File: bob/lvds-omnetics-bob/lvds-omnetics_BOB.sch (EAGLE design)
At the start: 33 parts, among them U1 SN65LVDS1, U2 SN65LVDS2, U3 SN65LVDS1, U4 SN65LVDS2, U5 SN65LVDS1, U6 SN65LVDS1

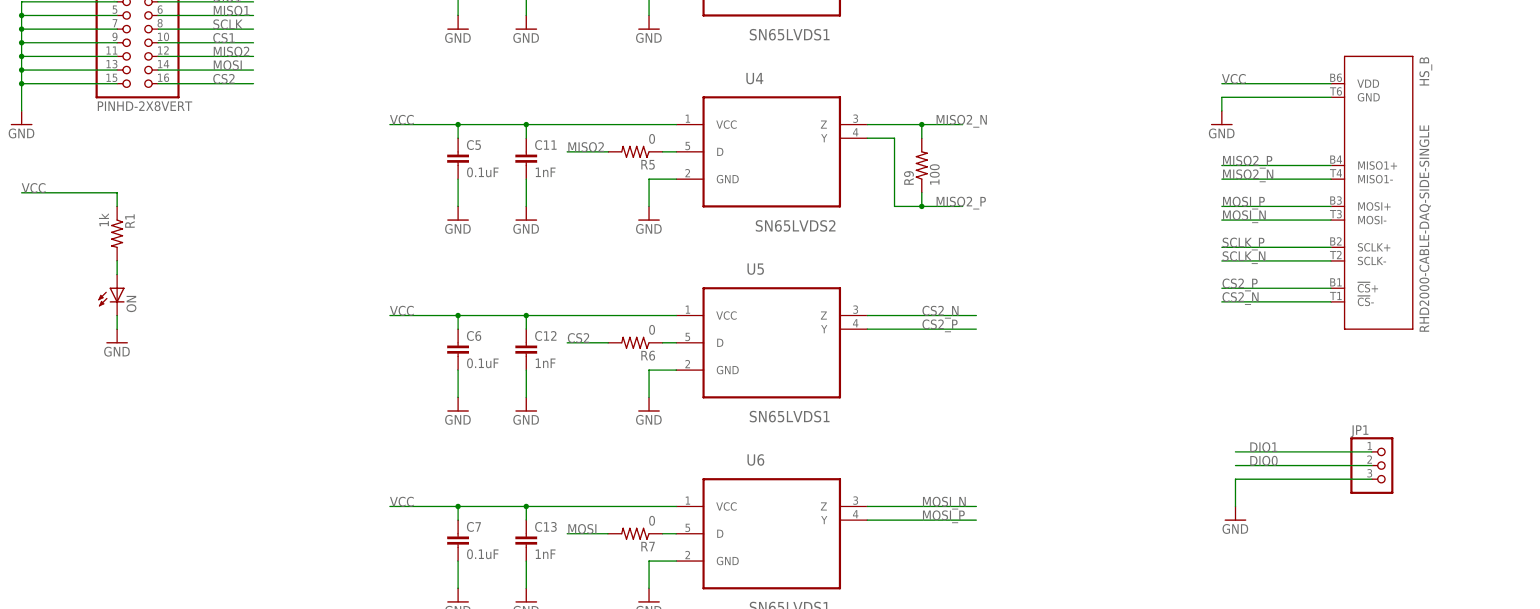
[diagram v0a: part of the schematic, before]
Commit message: Finished BOMs (and integrated parts into database) for all the BOBs. Now must do for the main board. Will take a while.
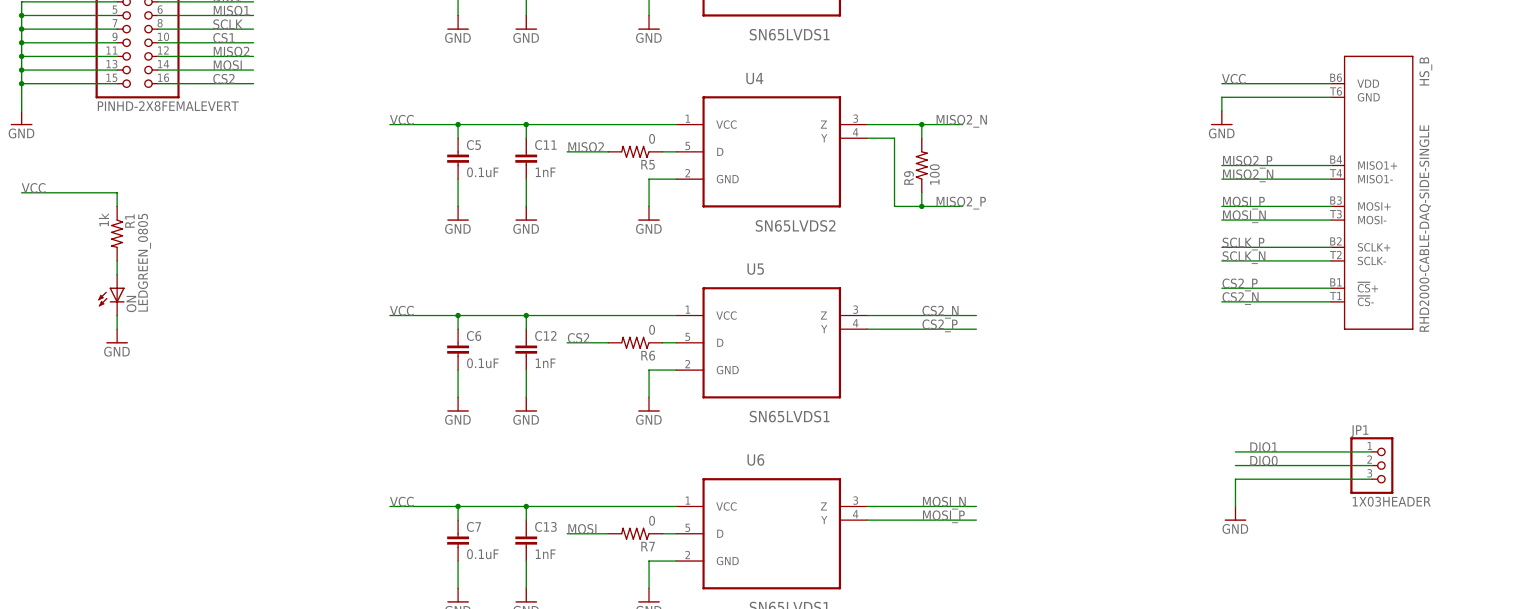
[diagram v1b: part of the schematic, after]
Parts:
- D_I/O: value PINHD-2X8VERT -> PINHD-2X8FEMALEVERT; device adafruit:PINHD-2X8VERT -> puggleboard:PINHD-2X8FEMALEVERT
- JP1: value (none) -> 1X03HEADER; device adafruit:PINHD-1X3 -> puggleboard:PINHD-1X3/90
- ON: value LED-CHIP0805 -> LEDGREEN_0805; device puggleboard:LED-CHIP0805 -> puggleboard:LEDGREEN_0805
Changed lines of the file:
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@@
 <part name="GND19" library="supply1" deviceset="GND" device=""/>
 <part name="R9" library="puggleboard" deviceset="R" device="_0603" value="100"/>
-<part name="D_I/O" library="adafruit" deviceset="PINHD-2X8" device="VERT" value="PINHD-2X8VERT"/>
+<part name="D_I/O" library="puggleboard" deviceset="PINHD-2X8" device="VERT" technology="FEMALE" value="PINHD-2X8FEMALEVERT"/>
 <part name="GND16" library="supply1" deviceset="GND" device=""/>
 <part name="GND20" library="supply1" deviceset="GND" device=""/>
@@
 <part name="R6" library="puggleboard" deviceset="R" device="_0603" value="0"/>
 <part name="R7" library="puggleboard" deviceset="R" device="_0603" value="0"/>
-<part name="JP1" library="adafruit" deviceset="PINHD-1X3" device=""/>
+<part name="JP1" library="puggleboard" deviceset="PINHD-1X3" device="" technology="/90" value="1X03HEADER"/>
 <part name="GND23" library="supply1" deviceset="GND" device=""/>
-<part name="ON" library="puggleboard" deviceset="LED" device="-CHIP0805" value=""/>
+<part name="ON" library="puggleboard" deviceset="LED" device="_0805" technology="GREEN" value="LEDGREEN_0805"/>
 <part name="R1" library="puggleboard" deviceset="R" device="_0603" value="1k"/>
 <part name="GND24" library="supply1" deviceset="GND" device=""/>
